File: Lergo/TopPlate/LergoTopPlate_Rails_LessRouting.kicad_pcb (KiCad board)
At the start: 2 copper layers, 164 x 146.3 mm, 69 parts, among them SW2 KEY_SWITCH, SW2 PRO MICRO

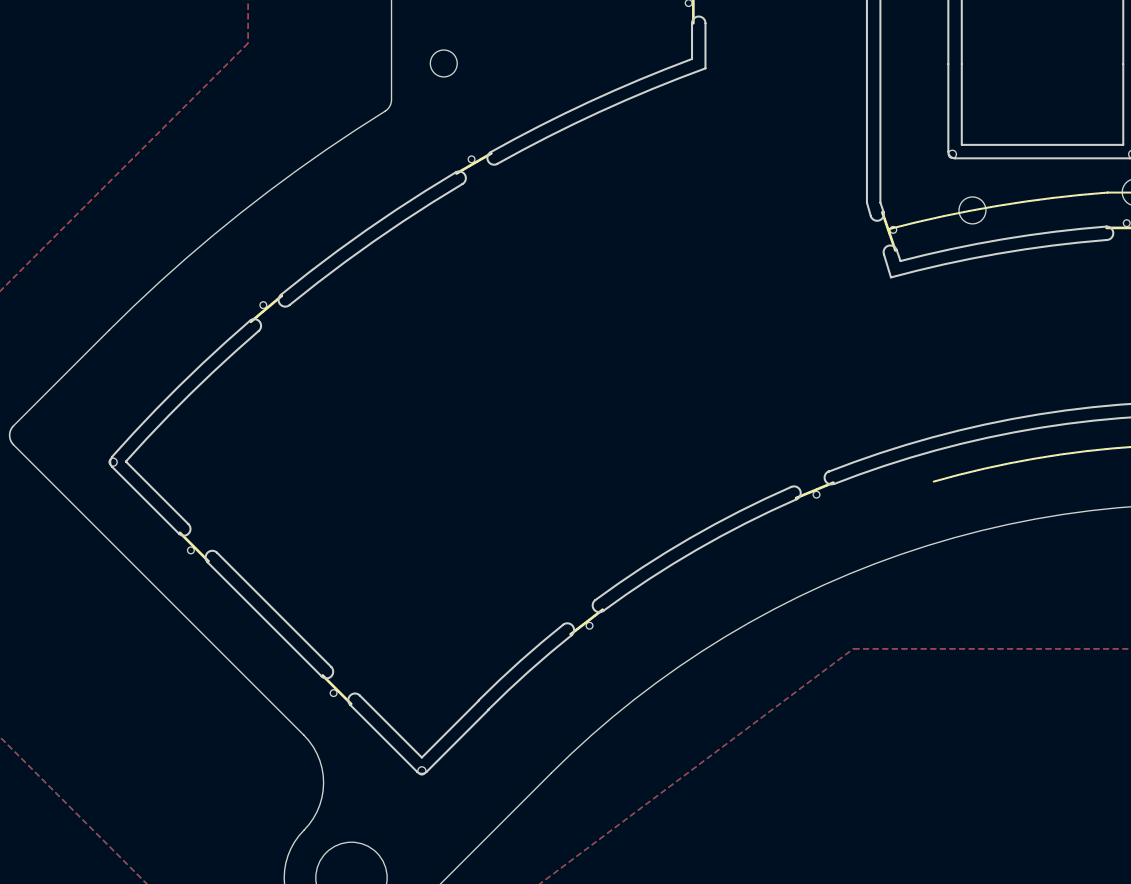
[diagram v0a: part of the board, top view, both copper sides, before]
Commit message: Integrating Pimoroni trackball in all top plates.
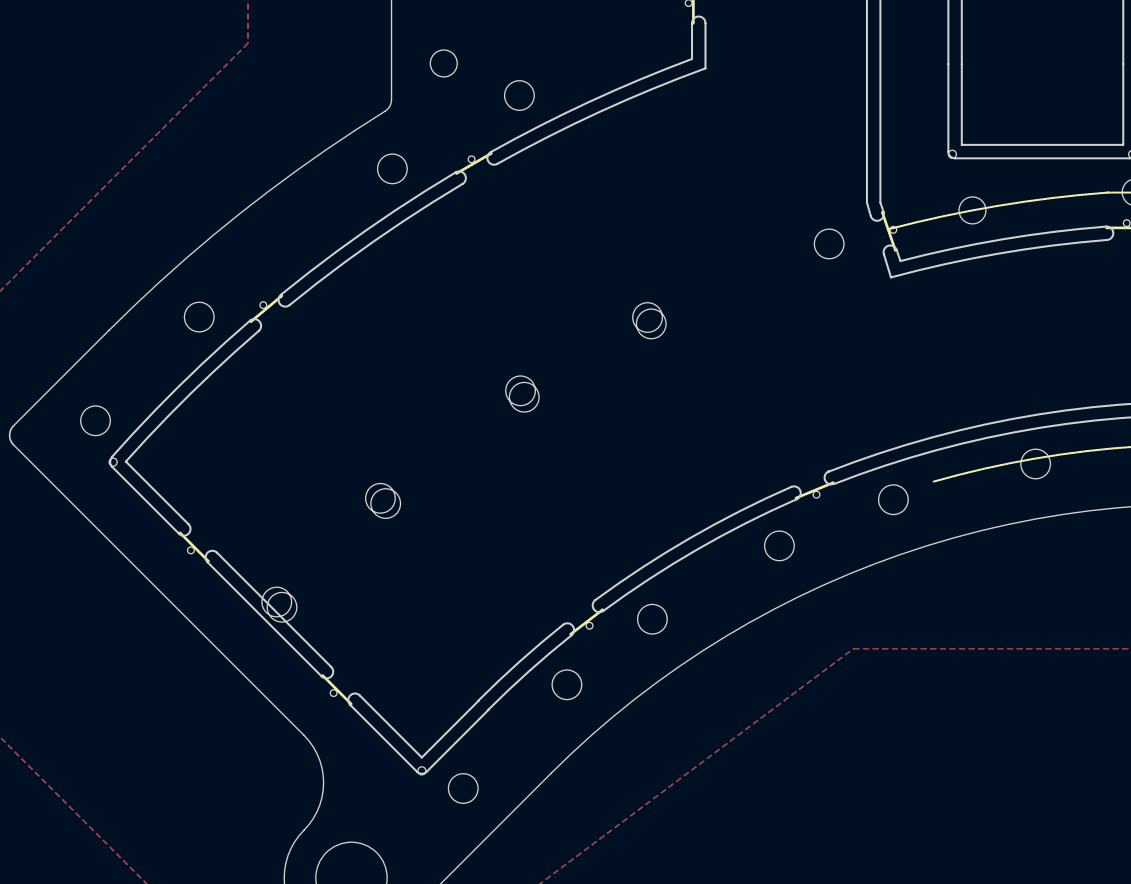
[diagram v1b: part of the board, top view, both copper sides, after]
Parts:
- added REF**: Pimoroni_Trackball, Lergo Footprints:Pimoroni_Trackball, F.Cu at (141.8, 120.6)
- added REF**: Pimoroni_Trackball, Lergo Footprints:Pimoroni_Trackball, F.Cu at (120.8, 129.1)
- added REF**: Pimoroni_Trackball, Lergo Footprints:Pimoroni_Trackball, F.Cu at (103.9, 142.1)
- added REF**: Pimoroni_Trackball, Lergo Footprints:Pimoroni_Trackball, F.Cu at (90.4, 128.6)
- added REF**: Pimoroni_Trackball, Lergo Footprints:Pimoroni_Trackball, F.Cu at (111.3, 112.6)
